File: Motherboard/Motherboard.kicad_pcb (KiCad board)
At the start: 4 copper layers, 50 x 36.6 mm, 74 parts, among them J1 USB-C In, J2 USB-C Split, J3 Pogo, J4 Conn_ARM_JTAG_SWD_10, Q1 AO3401A, Q3 AO3400A, Q4 AO3400A, SW1 Reset, U1 STM32G0B1CCU7, U2 LMV321, U3 TPD4E05U06, U4 TPD4E05U06, U5 XC6206P332MR, U6 TPS2553D

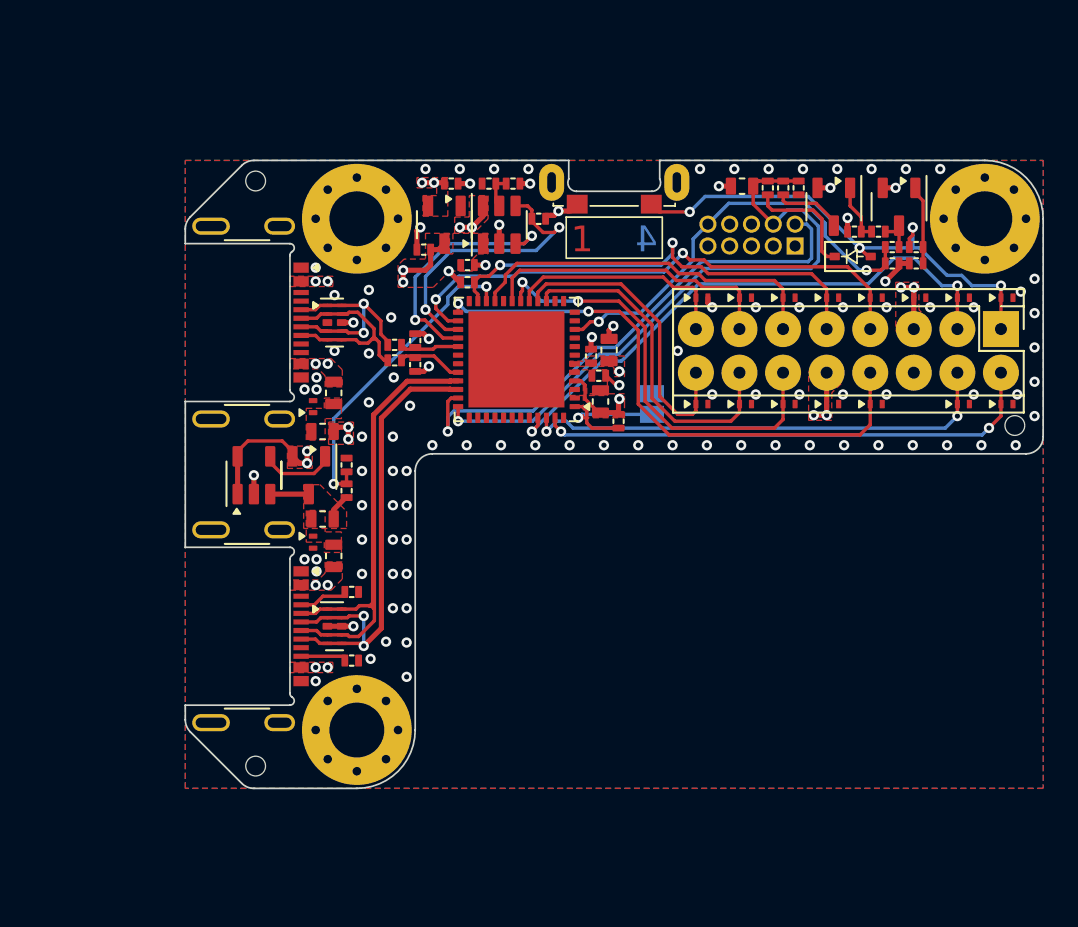
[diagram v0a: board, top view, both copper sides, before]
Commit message: 2026/09/26: V0.3 motherboard update complete
Reduced size again, rerouted board and changed shape slightly. Removed one mounting hole and centred the other between the USB ports. Changed input fuse and external +5V output to TPS2553-1 latching power switch with reverse voltage/current protection. Removed AO3401 and LMV321 discrete reverse current protection at VBUS input. Reduced size of VBUS and VSPLIT ferrite bead and transistors in the Acheron reset circuit. Made Acheron reset circuit reach DFU faster.
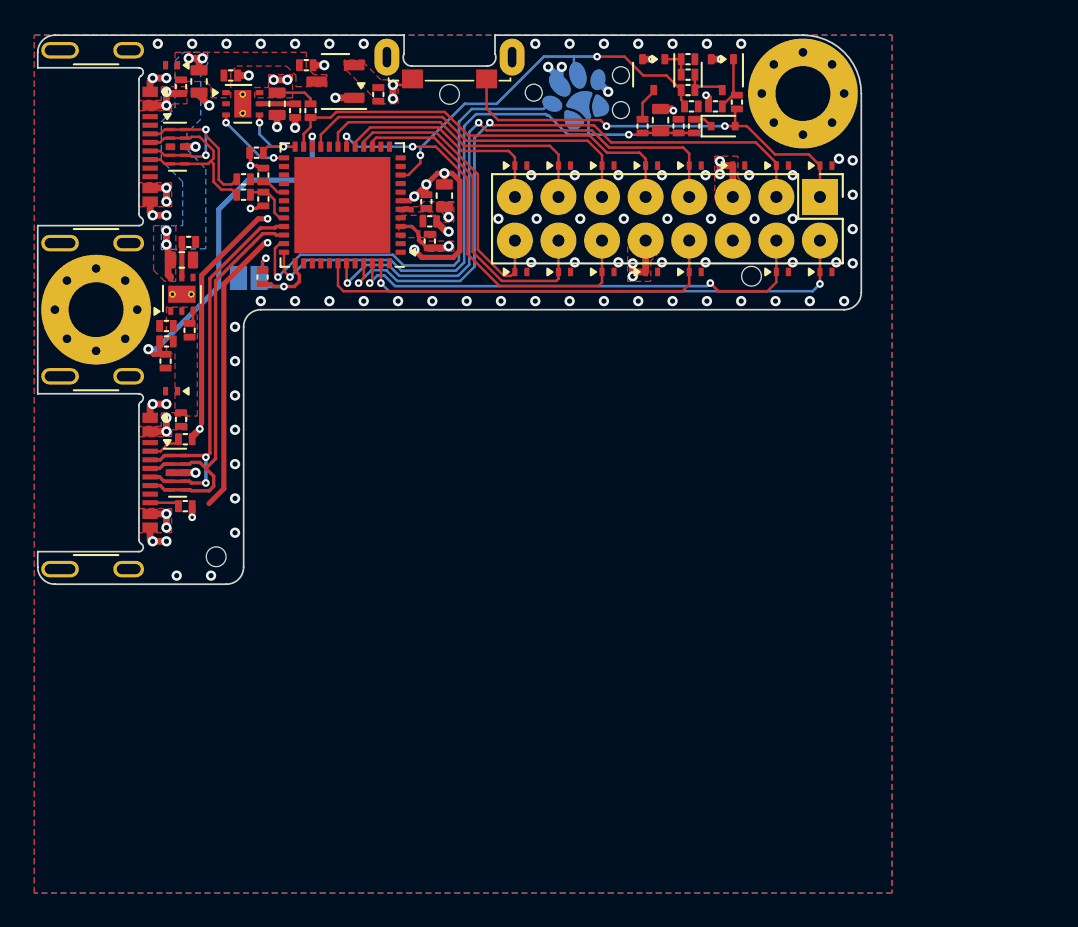
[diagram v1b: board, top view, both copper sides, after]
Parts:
- removed F1, F2: 500m, GB-Device:PTC_0603_1608Metric
- removed G***: Layer_Marker, GB-Misc:Layer_Marker
- removed H3: M3, GB-HolePad:MountingHole_3.2mm_M3_Pad_Via
- removed the J4 at (61.1, 30.3)
- removed Q3, Q4: AO3400A, GB-Package:SOT-23-3
- removed the R12 at (35.0, 44.5)
- removed the R13 at (35.0, 43.0)
- removed the R2 at (59.5, 26.9)
- removed the R20 at (46.2, 28.7)
- removed the R21 at (43.3, 26.6)
- removed the R22 at (44.7, 26.6)
- removed the U2 at (29.6, 43.6)
- removed the U6 at (43.9, 29.1)
- added C11: 10u, GB-Device:C_0603_1608Metric, F.Cu at (30.9, 22.0)
- added C12: 10u, GB-Device:C_0603_1608Metric, F.Cu at (26.4, 20.7)
- added C4: 100n, GB-Device:C_0402_1005Metric, F.Cu at (24.5, 35.0)
- added C5: 10u, GB-Device:C_0603_1608Metric, F.Cu at (25.4, 31.1)
- added J3: SWD, Paw-Connect:Paw-Connect_RevB_TC2030-IDC-NL_2x03_P1.27mm_Vertical, B.Cu at (48.5, 21.4)
- added Q2: 2N7002W, GB-Package:SOT-323_SC-70-3, F.Cu at (52.9, 20.3)
- added R17: 100k, GB-Device:R_0402_1005Metric, F.Cu at (54.9, 19.4)
- added R18: 100k, GB-Device:R_0402_1005Metric, F.Cu at (29.8, 24.9)
- added R19: 150k, GB-Device:R_0402_1005Metric, F.Cu at (32.0, 22.4)
- added R4: 100k, GB-Device:R_0402_1005Metric, F.Cu at (24.5, 35.9)
- added R5: 150k, GB-Device:R_0402_1005Metric, F.Cu at (24.4, 37.0)
- added R7: 100k, GB-Device:R_0402_1005Metric, F.Cu at (25.9, 35.2)
- added R9: 150k, GB-Device:R_0402_1005Metric, F.Cu at (55.2, 23.3)
- added U3: TPS2553-1, GB-Package:WSON-6-1EP_2x2mm_P0.65mm_EP1x1.6mm, F.Cu at (25.4, 33.1)
- added U4: XC6206P332MR, GB-Package:SOT-23-3, F.Cu at (34.4, 20.7)
- D2: renamed from D1; value 1N4148 -> 1N4148WT; footprint GB-Device:D_SOD-323 -> GB-Device:D_SOD-523
- FB1: renamed from FB3; value 150@100 -> 120@100; footprint GB-Device:L_0603_1608Metric -> GB-Device:L_0402_1005Metric
- FB2: renamed from FB1; value 150@100 -> 120@100; footprint GB-Device:L_0603_1608Metric -> GB-Device:L_0402_1005Metric
- FB3: renamed from FB2; value 150@100 -> 120@100; footprint GB-Device:L_0603_1608Metric -> GB-Device:L_0402_1005Metric
- J1: footprint GB-Connector:USB_C_Receptacle_HRO_TYPE-C-31-M-13x -> GB-Connector:USB_C_Receptacle_Molex_2169900001
- J4: renamed from J3; footprint GB-Header:Connector_2x08_2.54mm_MillMax_Pogo_Target_419-10-216-00-001000-Double_Sided -> GB-Header:PinHeader_2x08_2.54mm_MillMax_PogoTarget_419-10-216-00-001000-Double_Sided
- J5: renamed from J2; footprint GB-Connector:USB_C_Receptacle_HRO_TYPE-C-31-M-13x -> GB-Connector:USB_C_Receptacle_Molex_2169900001
- Q1: value AO3401A -> 2N7002W; footprint GB-Package:SOT-23-3 -> GB-Package:SOT-323_SC-70-3
- R8: value 100k -> 56k
- U5: value XC6206P332MR -> TPS2553-1; footprint GB-Package:SOT-23-3 -> GB-Package:WSON-6-1EP_2x2mm_P0.65mm_EP1x1.6mm
- moved TOOL2 47.2 mm to (27.4, 48.4)
- moved TOOL3 40.6 mm to (58.6, 32.0), turned to 0 degrees
- moved R8 38.8 mm to (25.8, 30.1)
- moved Q1 33.6 mm to (56.9, 20.3)
- moved H1 28.8 mm to (20.4, 34.0)
- moved H2 27.0 mm to (61.6, 21.4)
- moved JP1 24.6 mm to (29.3, 32.1), turned to 180 degrees
- moved R1 22.4 mm to (30.1, 32.1)
- moved FB3 21.7 mm to (25.4, 21.0), turned to -90 degrees
- moved D5 21.5 mm to (24.8, 19.8), turned to 180 degrees
- moved C8 17.7 mm to (28.2, 20.4)
- moved R14 15.0 mm to (54.9, 21.2)
- moved R12 14.9 mm to (56.5, 22.1)
- moved C10 14.9 mm to (55.1, 22.1)
- moved R13 14.4 mm to (54.9, 20.3)
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- renumbered C3 to C1, C5 to C10, C1 to C2, C2 to C3, C4 to C9, D2 to D1, D11 to D10, D6 to D11, D14 to D12, D17 to D13, D18 to D14, D12 to D17, D13 to D18, D4 to D3, D5 to D4, D3 to D5, D7 to D6, D8 to D7, D9 to D8, D10 to D9, R18 to R1, R3 to R10, R4 to R11, R5 to R12, R6 to R13, R7 to R14, R14 to R15, R15 to R16, R10 to R2, R16 to R20, R17 to R21, R9 to R22, R11 to R3, R19 to R6, U3 to U1, U1 to U2, U4 to U6
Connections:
- net CC1 renamed Net-(J1-CC1)
- net CC2 renamed Net-(J1-CC2)
- net SPLIT_RX renamed USART1_SPLIT_RX
- net SPLIT_TX renamed USART1_SPLIT_TX
- net USART1_RX renamed USART1_MCU_RX
- net USART1_TX renamed USART1_MCU_TX
- D1 pad 1: /VBUS_FUSED -> /VBUS_FERRITE
- D5 pad 1: /VSPLIT_FUSED -> VBUS
- FB2 pad 1: /VBUS_FUSED -> /VBUS_RAW
- FB3 pad 2: /VSPLIT_FUSED -> /VSPLIT_RAW
- Q1 pad 2: VBUS -> GND
- Q1 pad 3: /VBUS_FERRITE -> Net-(Q1-D)
- R10 pad 2: Net-(Q4-G) -> Net-(Q1-G)
- R12 pad 1: Net-(Q4-G) -> Net-(Q1-G)
- R13 pad 1: Net-(Q4-D) -> Net-(Q1-D)
- R13 pad 2: Net-(Q3-G) -> Net-(Q2-G)
- R14 pad 1: Net-(Q4-D) -> Net-(Q1-D)
- R8 pad 1: GND -> Net-(U3-ILIM)
- R8 pad 2: Net-(Q3-G) -> GND
- U2 pad 1: SPLIT_SIDE -> unconnected-(U2-PC13-Pad1)
- U2 pad 24: unconnected-(U1-PB12-Pad24) -> ~{RGB_FAULT}
- U2 pad 25: I2C2_SCL -> RGB_EN
- U2 pad 26: I2C2_SDA -> unconnected-(U2-PB14-Pad26)
- U2 pad 27: ~{RGB_FAULT} -> unconnected-(U2-PB15-Pad27)
- U2 pad 28: RGB_EN -> unconnected-(U2-PA8-Pad28)
- U2 pad 37: unconnected-(U1-PA15-Pad37) -> SPLIT_SIDE
- U2 pad 42: unconnected-(U1-PB3-Pad42) -> I2C2_SCL
- U2 pad 43: unconnected-(U1-PB4-Pad43) -> I2C2_SDA
- U5 pad 1: GND -> VBUS
- U5 pad 2: +3V3 -> GND
- U5 pad 3: VBUS -> RGB_EN
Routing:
- net GND: track 15.8 -> 62.3 mm, vias 103 -> 98
- net ~{RGB_FAULT}: track 16.8 -> 4.78 mm
- net RGB_EN: track 14.4 -> 4.67 mm
- net VBUS: track 13.5 -> 4.41 mm, vias 6 -> 4
- net I2C2_SCL: track 33.5 -> 24.6 mm, vias 2 -> 0
- net Net-(D2-K): track 6.88 -> 1.17 mm
- net /VSPLIT_RAW: track 0.00 -> 4.39 mm
- net Net-(Q4-G): track 4.29 -> 0.00 mm
- net GPIO3_POGO: track 33.1 -> 37.4 mm
- net /VBUS_FERRITE: track 3.81 -> 0.00 mm
- net /VBUS_RAW: track 0.00 -> 3.50 mm
- net Net-(Q3-G): track 3.42 -> 0.00 mm
- net SPLIT_SIDE: track 8.36 -> 5.15 mm
- net SWDIO: track 31.1 -> 28.0 mm
- net USB_D-: track 27.6 -> 24.7 mm, vias 0 -> 2
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- added copper zone on B.Cu, net VBUS
- removed copper zone on F.Cu, net /VBUS_FUSED
- removed copper zone on F.Cu, net /VSPLIT_FUSED
- removed copper zone on In2.Cu, net VBUS
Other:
- board size 50 x 36.6 mm -> 48 x 32 mm
- board text added: "Solder if RHS"
- board text added: "V0.3"
- board text removed: "SWITCH"
- board text removed: "Solder if this side up"
- board text removed: "V0.2"
